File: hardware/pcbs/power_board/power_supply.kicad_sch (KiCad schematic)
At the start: 27 parts, among them J15 PJ-102AH, U12 LMR38020, U13 LMR38020

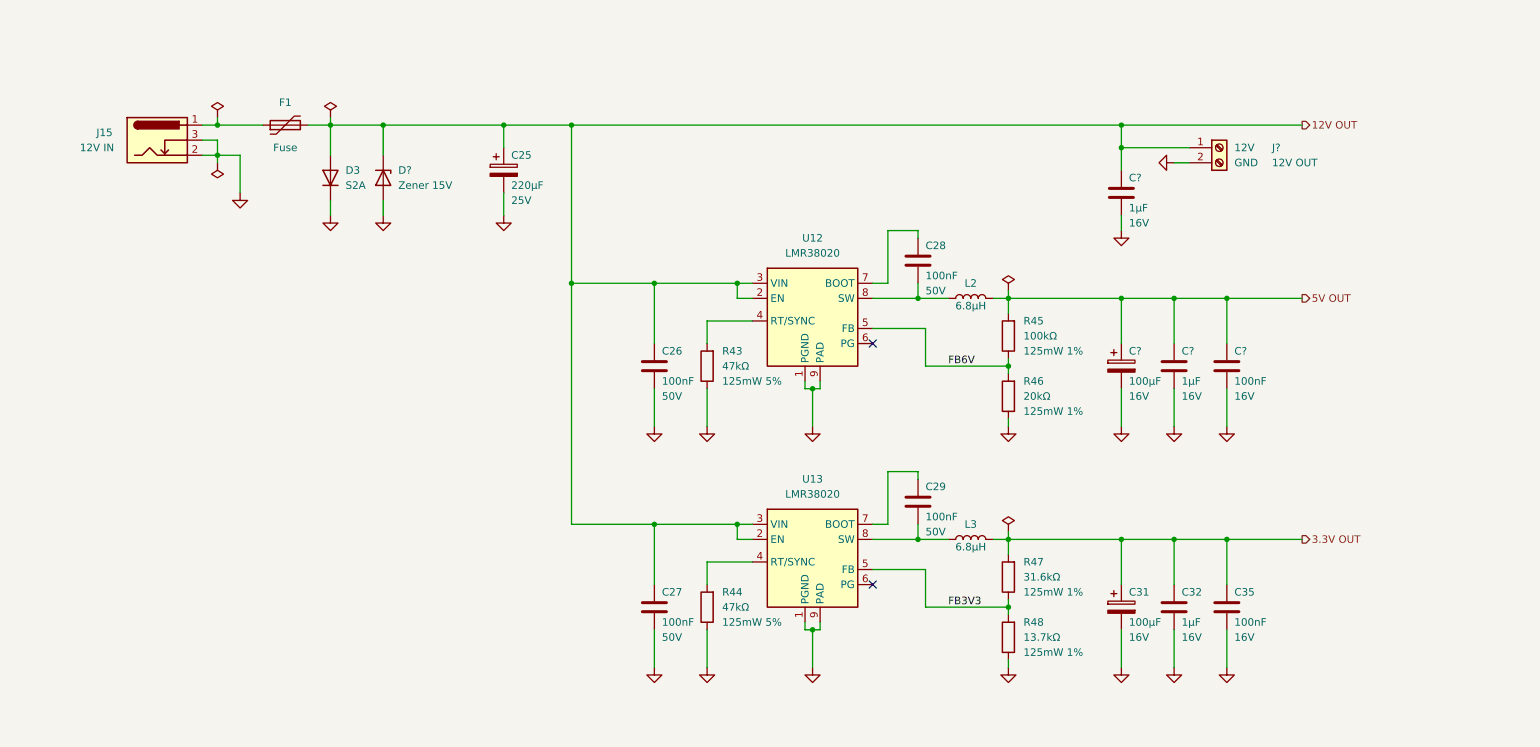
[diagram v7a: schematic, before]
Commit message: power_board: update components to new versions and annotate
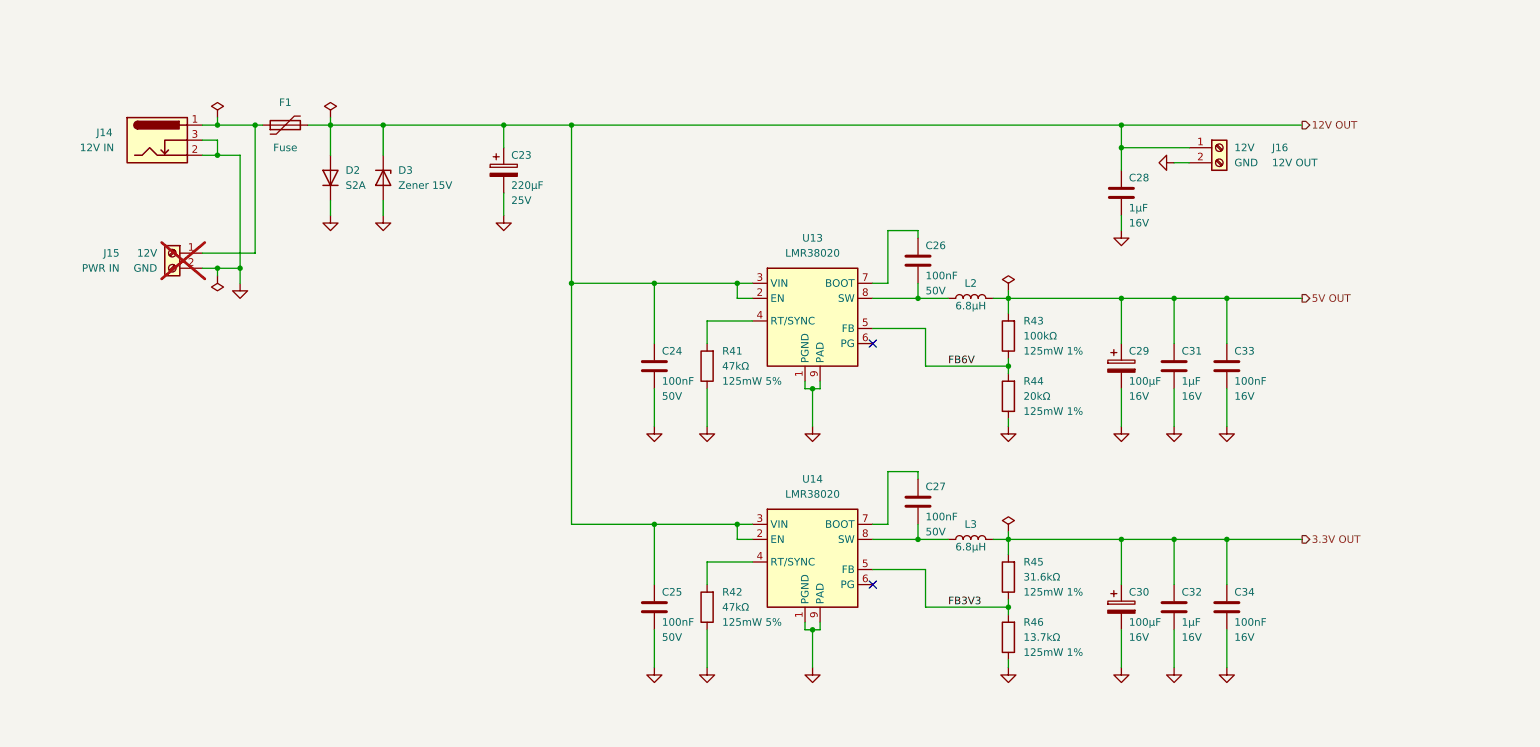
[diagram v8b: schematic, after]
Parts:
- added J15: ScrewTerminal_02, conn:TerminalBlock_4Ucon_1x02_P3.50mm_Vertical, symbol conn:Screw_Terminal_01x02
- D2: renamed from D3; Part (none) -> S2A
- F1: footprint conn:Fuseholder_Littelfuse_625_series_5x20mm -> conn:Fuseholder_FS002; Part (none) -> 2x FS-002; Shop https://eu.mouser.com/ProductDetail/Littelfuse/65600001409?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 -> 2x https://store.comet.bg/Catalogue/Product/51167/
- J14: renamed from J15; value PJ-102AH -> Barrel Jack; footprint Connector_BarrelJack:BarrelJack_CUI_PJ-102AH_Horizontal -> Connector_BarrelJack:BarrelJack_Horizontal; Part (none) -> YDJ-1134; Shop https://eu.mouser.com/ProductDetail/CUI-Devices/PJ-102AH?qs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 -> https://store.comet.bg/Catalogue/Product/29148/
- J16: renamed from J?; Part (none) -> 15EDGVC-3.5-02P-14-00AH and 15EDGKA-3.5-02P-14-100AH; Shop https://eu.mouser.com/ProductDetail/TE-Connectivity/284514-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 -> https://store.comet.bg/Catalogue/Product/45040/ and https:/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
- L2, L3: Part (none) -> NRS5030T6R8MMGJ
- U13: renamed from U12; Part (none) -> LMR38020FSDDAR; Shop https://www.mouser.bg/ProductDetail/Texas-Instruments/LMR38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 -> https://eu.mouser.com/ProductDetail/Texas-Instruments/LMR38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
- U14: renamed from U13; Part (none) -> LMR38020FSDDAR; Shop https://www.mouser.bg/ProductDetail/Texas-Instruments/LMR38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 -> https://eu.mouser.com/ProductDetail/Texas-Instruments/LMR38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
- gave numbers to parts that had none: 5
- renumbered C25 to C23, C26 to C24, C27 to C25, C28 to C26, C29 to C27, C31 to C30, C35 to C34, R43 to R41, R44 to R42, R45 to R43, R46 to R44, R47 to R45, R48 to R46
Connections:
- net GND: now also J15.2 (Pin_2)
- net at F1.1, J14.1: now also J15.1 (Pin_1)
